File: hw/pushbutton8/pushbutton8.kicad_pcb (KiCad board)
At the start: 2 copper layers, 70 x 70 mm, 34 parts, among them U1 74HC595

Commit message: Added first iteration of rev B  - usable with Reb B and newer bus-modules which have 24V on header
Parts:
- moved C1 1.91 mm to (121.9, 124.5)
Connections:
- MOD1 pad 3: Net-(C1-Pad1) -> (no net)
- MOD1 pad 4: Net-(C1-Pad1) -> (no net)
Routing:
- net Net-(C1-Pad1): track 59.6 -> 30.2 mm, vias 0 -> 1
- net Net-(D4-Pad1): track 38.7 -> 39.8 mm
- net Net-(D5-Pad1): track 13.8 -> 12.9 mm
- net Net-(C1-Pad2): track 245.8 -> 246.6 mm
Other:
- board text added: "03/2018"
- board text added: "PushButton8 - Rev. 2"

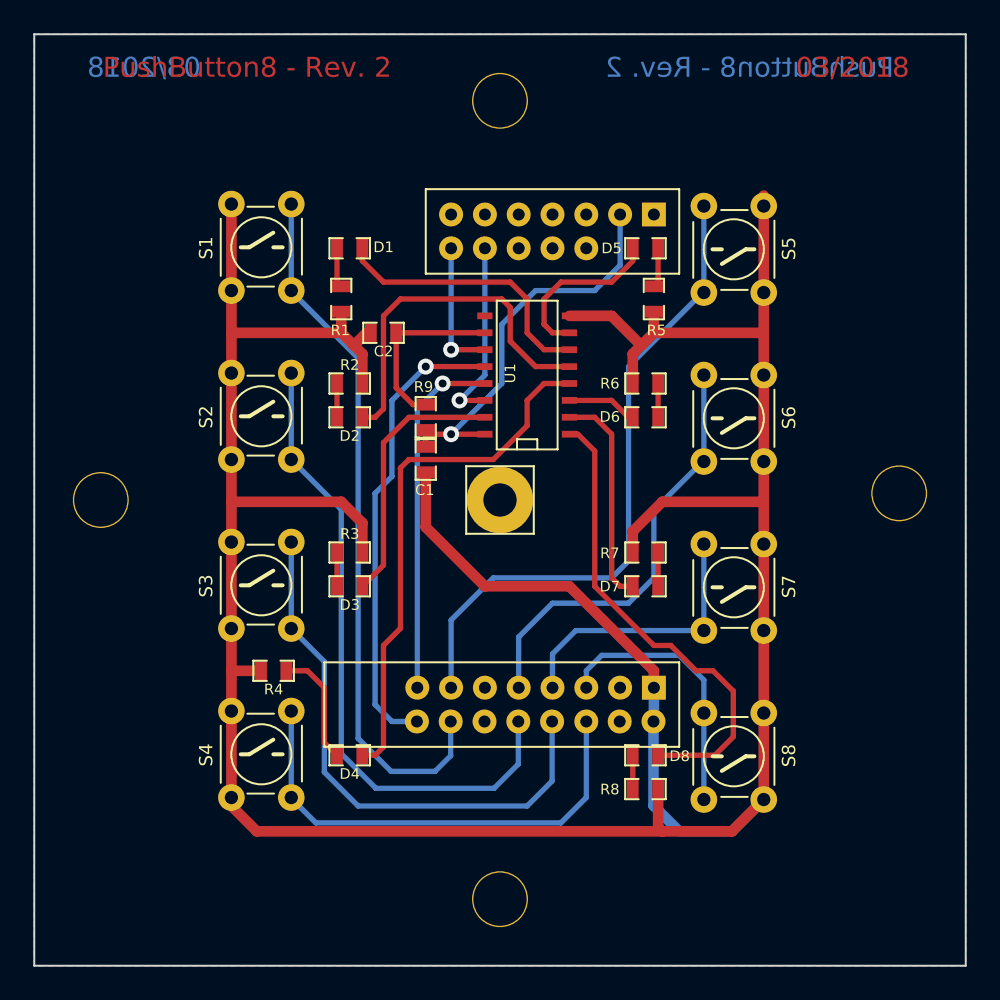
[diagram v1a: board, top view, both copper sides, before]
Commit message: New hw pushbutton8 rev.3: New KiCAD file types and PCB
- PCB with ground planes instead of unconnected copper islands.
- Update to KiCAD 6 file format.
- Reorganization of PDF files (rev1..3 preproduction, revA will be the first official).
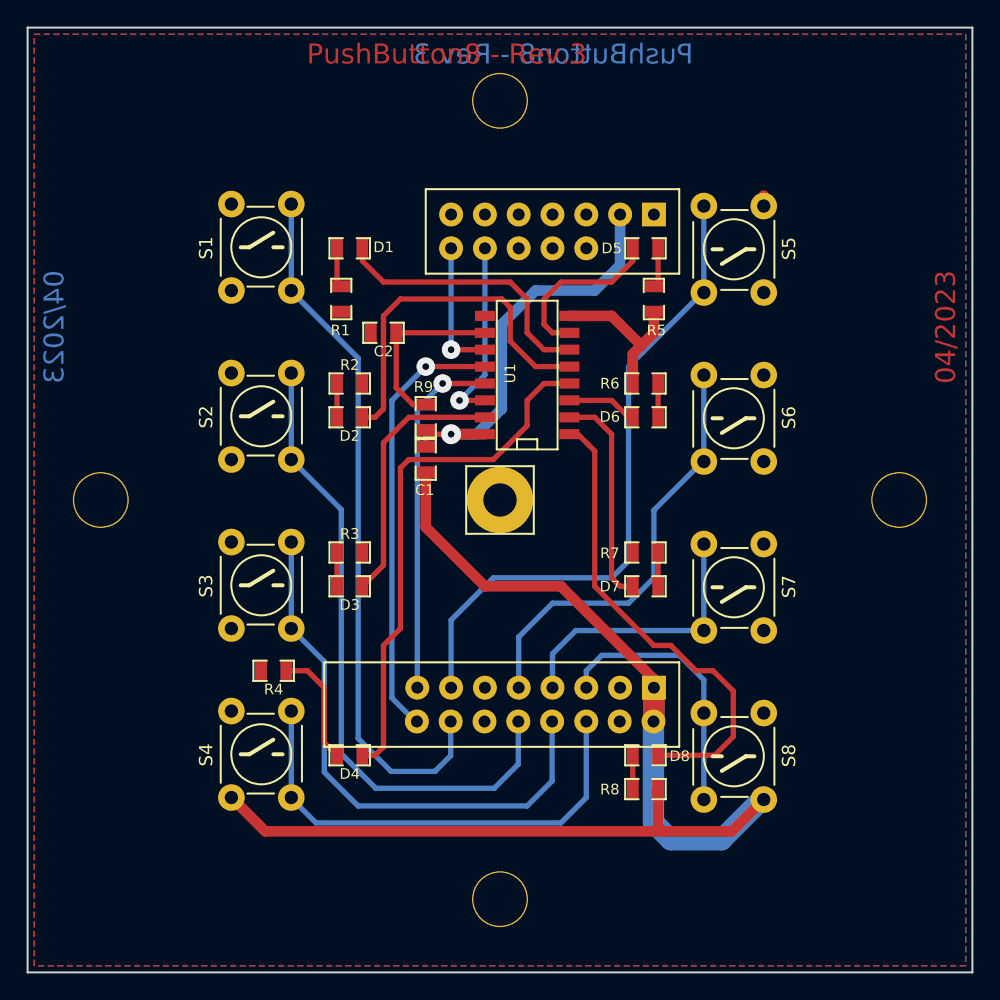
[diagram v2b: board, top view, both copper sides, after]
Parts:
- moved H3 0.50 mm to (157.5, 127.5)
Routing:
- net Net-(C1-Pad2): track 246.6 -> 109.0 mm
- net Net-(MOD1-Pad16): track 35.8 -> 33.7 mm
- net Net-(C1-Pad1): track 30.2 -> 31.3 mm
- added copper zone on B.Cu, net Net-(C1-Pad1)
- added copper zone on F.Cu, net Net-(C1-Pad2)
- removed copper zone on B.Cu, net (none)
- removed copper zone on F.Cu, net (none)
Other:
- board size 70 x 70 mm -> 71 x 71 mm
- net class Default removed
- net class Power removed
- board text added: "04/2023"
- board text added: "PushButton8 - Rev.3"
- board text removed: "03/2018"
- board text removed: "PushButton8 - Rev. 2"

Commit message: pushbutton8 rev.3: Curved slotted holes and enhanced circuit track routing.
This variant has been prototyped at home and tested successfully in Nov. 2023.
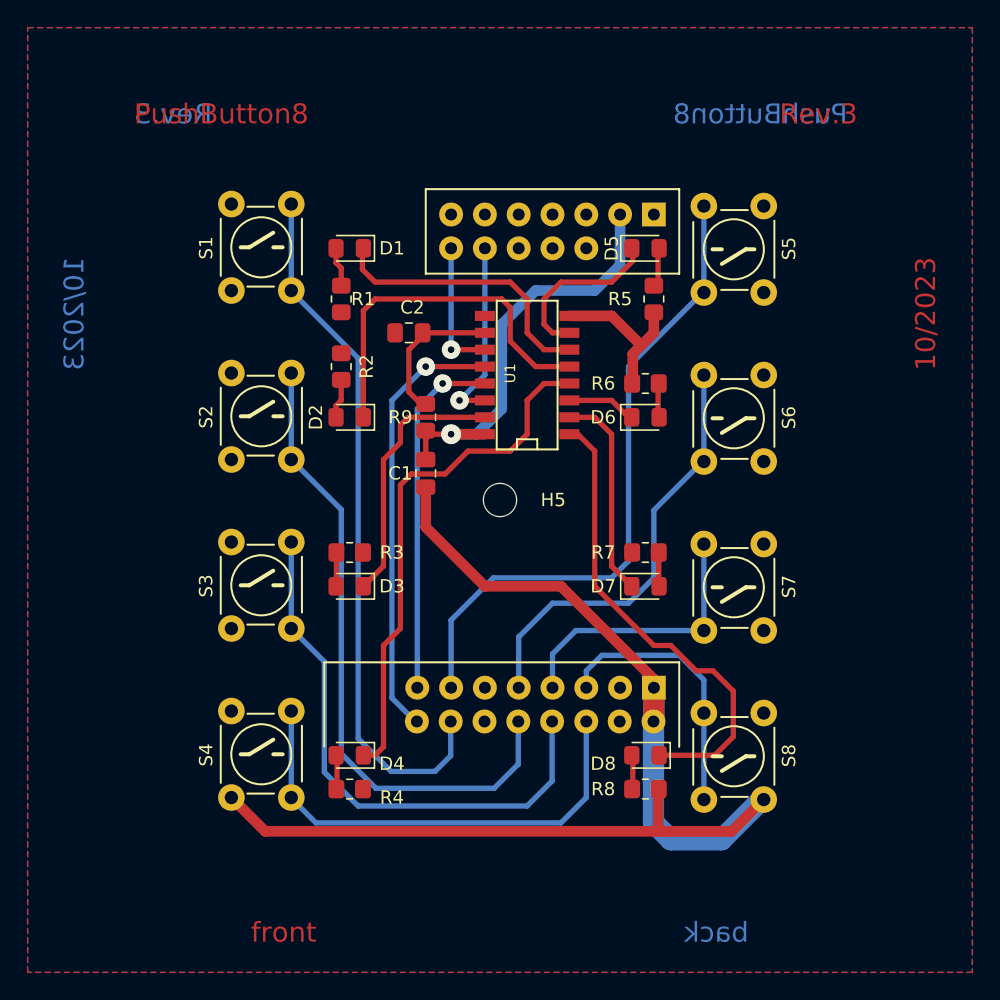
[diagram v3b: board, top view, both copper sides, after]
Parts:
- removed H1, H2, H3, H4: HOLE, Mechanical:HOLE_4,0mm
- C1, C2: footprint Capacitors_SMD:C_0805 -> Capacitor_SMD:C_0805_2012Metric_Pad1.18x1.45mm_HandSolder
- D1, D2, D3, D4, D5, D6, D7, D8: footprint Resistor:R_0805 -> LED_SMD:LED_0805_2012Metric_Pad1.15x1.40mm_HandSolder
- H5: footprint Mechanical:HOLE_2.5mm -> MountingHole:MountingHole_2.5mm
- R1, R2, R3, R4, R5, R6, R7, R8, R9: footprint Resistor:R_0805 -> Resistor_SMD:R_0805_2012Metric_Pad1.20x1.40mm_HandSolder
- moved R4 10.6 mm to (116.2, 149.2), turned to 0 degrees
- moved C2 1.91 mm to (120.7, 114.9)
- moved R2 1.42 mm to (115.6, 117.5), turned to 90 degrees
- moved C1 1.04 mm to (121.9, 125.5)
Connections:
- MOD1 pad 12: (no net) -> unconnected-(MOD1-Pad12)
- MOD1 pad 21: (no net) -> unconnected-(MOD1-Pad21)
- MOD1 pad 25: (no net) -> unconnected-(MOD1-Pad25)
- MOD1 pad 26: (no net) -> unconnected-(MOD1-Pad26)
- MOD1 pad 27: (no net) -> unconnected-(MOD1-Pad27)
- MOD1 pad 28: (no net) -> unconnected-(MOD1-Pad28)
- MOD1 pad 29: (no net) -> unconnected-(MOD1-Pad29)
- MOD1 pad 3: (no net) -> unconnected-(MOD1-Pad3)
- MOD1 pad 30: (no net) -> unconnected-(MOD1-Pad30)
- MOD1 pad 31: (no net) -> unconnected-(MOD1-Pad31)
- MOD1 pad 33: (no net) -> unconnected-(MOD1-Pad33)
- MOD1 pad 4: (no net) -> unconnected-(MOD1-Pad4)
- U1 pad 9: (no net) -> unconnected-(U1-Pad9)
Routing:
- net Net-(D4-Pad2): track 8.86 -> 2.54 mm
- net Net-(C2-Pad1): track 13.5 -> 11.1 mm
- net Net-(C1-Pad2): track 109.0 -> 106.5 mm
- net Net-(MOD1-Pad14): track 54.0 -> 53.3 mm
- net Net-(MOD1-Pad16): track 33.7 -> 33.0 mm
- net Net-(MOD1-Pad15): track 27.5 -> 26.8 mm
- net Net-(MOD1-Pad6): track 36.6 -> 36.0 mm
- net Net-(D7-Pad1): track 16.3 -> 15.8 mm
- net Net-(D2-Pad1): track 26.9 -> 27.5 mm
- added copper zone on B.Cu, net Net-(C1-Pad2)
- removed copper zone on B.Cu, net Net-(C1-Pad1)
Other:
- board outline removed
- board text added: "10/2023"
- board text added: "PushButton8"
- board text added: "Rev.3"
- board text added: "back"
- board text added: "front"
- board text removed: "04/2023"
- board text removed: "PushButton8 - Rev.3"

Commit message: pusbutton8: create gerber files
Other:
- board outline added: 68 x 68 mm
